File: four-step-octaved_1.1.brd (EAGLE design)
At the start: 94.3 x 44.4 mm, 39 parts, among them IC1 556, IC2 4017N, IC3 4040N, J1 -BATTERY+, J2 SPEAKER, U1 LM386N

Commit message: Rename RV to VR to match waltron
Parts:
- renumbered RV1 to VR1, RV2 to VR2, RV3 to VR3, RV4 to VR4, RV5 to VR5
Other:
- board text added: "VR1"
- board text added: "VR2"
- board text added: "VR3"
- board text added: "VR4"
- board text added: "VR5"
- board text added: "VR6"
- board text removed: "RV1"
- board text removed: "RV2"
- board text removed: "RV3"
- board text removed: "RV4"
- board text removed: "RV5"
- board text removed: "RV6"
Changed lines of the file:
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@@
 <text x="45.085" y="35.56" size="0.8128" layer="21" font="vector">C2</text>
 <text x="45.72" y="20.0025" size="0.8128" layer="21" font="vector">C3</text>
-<text x="82.55" y="37.7825" size="0.8128" layer="21" font="vector">RV1</text>
-<text x="82.8675" y="26.67" size="0.8128" layer="21" font="vector">RV6</text>
-<text x="17.145" y="7.9375" size="0.8128" layer="21" font="vector">RV2</text>
-<text x="32.7025" y="7.9375" size="0.8128" layer="21" font="vector">RV3</text>
-<text x="64.4525" y="7.9375" size="0.8128" layer="21" font="vector">RV5</text>
-<text x="48.5775" y="7.9375" size="0.8128" layer="21" font="vector">RV4</text>
+<text x="82.55" y="37.7825" size="0.8128" layer="21" font="vector">VR1</text>
+<text x="82.8675" y="26.67" size="0.8128" layer="21" font="vector">VR6</text>
+<text x="17.145" y="7.9375" size="0.8128" layer="21" font="vector">VR2</text>
+<text x="32.7025" y="7.9375" size="0.8128" layer="21" font="vector">VR3</text>
+<text x="64.4525" y="7.9375" size="0.8128" layer="21" font="vector">VR5</text>
+<text x="48.5775" y="7.9375" size="0.8128" layer="21" font="vector">VR4</text>
 <text x="62.865" y="31.115" size="0.8128" layer="21" font="vector">C5</text>
 <text x="84.7725" y="31.115" size="0.8128" layer="21" font="vector">TEMPO</text>
@@
 <attribute name="PROD_ID" value="RES-12182" x="67.6275" y="21.9075" size="1.778" layer="27" rot="R270" display="off"/>
 </element>
-<element name="RV1" library="SparkFun-Retired" package="TRIM_POT" value="50K" x="86.36" y="33.655" smashed="yes" rot="R90">
+<element name="VR1" library="SparkFun-Retired" package="TRIM_POT" value="50K" x="86.36" y="33.655" smashed="yes" rot="R90">
 <attribute name="PROD_ID" value="COM-00104" x="86.36" y="33.655" size="1.778" layer="27" rot="R90" display="off"/>
 </element>
-<element name="RV2" library="SparkFun-Retired" package="TRIM_POT" value="50K" x="15.24" y="3.175" smashed="yes" rot="R90">
+<element name="VR2" library="SparkFun-Retired" package="TRIM_POT" value="50K" x="15.24" y="3.175" smashed="yes" rot="R90">
 <attribute name="PROD_ID" value="COM-00104" x="15.24" y="3.175" size="1.778" layer="27" rot="R90" display="off"/>
 </element>
-<element name="RV3" library="SparkFun-Retired" package="TRIM_POT" value="50K" x="31.115" y="3.175" smashed="yes" rot="R90">
+<element name="VR3" library="SparkFun-Retired" package="TRIM_POT" value="50K" x="31.115" y="3.175" smashed="yes" rot="R90">
 <attribute name="PROD_ID" value="COM-00104" x="31.115" y="3.175" size="1.778" layer="27" rot="R90" display="off"/>
 </element>
-<element name="RV4" library="SparkFun-Retired" package="TRIM_POT" value="50K" x="46.99" y="3.175" smashed="yes" rot="R90">
+<element name="VR4" library="SparkFun-Retired" package="TRIM_POT" value="50K" x="46.99" y="3.175" smashed="yes" rot="R90">
 <attribute name="PROD_ID" value="COM-00104" x="46.99" y="3.175" size="1.778" layer="27" rot="R90" display="off"/>
 </element>
-<element name="RV5" library="SparkFun-Retired" package="TRIM_POT" value="50K" x="62.865" y="3.175" smashed="yes" rot="R90">
+<element name="VR5" library="SparkFun-Retired" package="TRIM_POT" value="50K" x="62.865" y="3.175" smashed="yes" rot="R90">
 <attribute name="PROD_ID" value="COM-00104" x="62.865" y="3.175" size="1.778" layer="27" rot="R90" display="off"/>
 </element>
@@
 <signal name="N$1" class="1">
 <contactref element="R1" pad="P$2"/>
-<contactref element="RV1" pad="3"/>
+<contactref element="VR1" pad="3"/>
 <wire x1="88.9" y1="33.655" x2="29.21" y2="27.6225" width="0" layer="19" extent="1-1"/>
 </signal>
 <signal name="N$2" class="1">
 <contactref element="IC1" pad="1"/>
-<contactref element="RV1" pad="2"/>
-<contactref element="RV1" pad="1"/>
+<contactref element="VR1" pad="2"/>
+<contactref element="VR1" pad="1"/>
 <contactref element="R2" pad="P$1"/>
 <wire x1="21.59" y1="30.7975" x2="32.0675" y2="35.56" width="0" layer="19" extent="1-1"/>
@@
 <signal name="N$9" class="1">
 <contactref element="IC2" pad="4"/>
-<contactref element="RV4" pad="3"/>
+<contactref element="VR4" pad="3"/>
 <contactref element="R7" pad="P$2"/>
 <wire x1="49.53" y1="3.175" x2="48.26" y2="10.795" width="0" layer="19" extent="1-1"/>
@@
 <signal name="N$10" class="1">
 <contactref element="IC2" pad="7"/>
-<contactref element="RV5" pad="3"/>
+<contactref element="VR5" pad="3"/>
 <contactref element="R8" pad="P$2"/>
 <wire x1="65.405" y1="3.175" x2="64.135" y2="10.795" width="0" layer="19" extent="1-1"/>
@@
 <signal name="N$7" class="1">
 <contactref element="IC2" pad="3"/>
-<contactref element="RV2" pad="3"/>
+<contactref element="VR2" pad="3"/>
 <contactref element="R5" pad="P$2"/>
 <wire x1="16.51" y1="10.795" x2="4.7625" y2="31.75" width="0" layer="19" extent="1-1"/>
@@
 <signal name="N$8" class="1">
 <contactref element="IC2" pad="2"/>
-<contactref element="RV3" pad="3"/>
+<contactref element="VR3" pad="3"/>
 <contactref element="R6" pad="P$2"/>
 <wire x1="33.655" y1="3.175" x2="32.385" y2="10.795" width="0" layer="19" extent="1-1"/>
@@
 </signal>
 <signal name="N$11" class="1">
-<contactref element="RV2" pad="1"/>
-<contactref element="RV2" pad="2"/>
+<contactref element="VR2" pad="1"/>
+<contactref element="VR2" pad="2"/>
 <contactref element="D1" pad="A"/>
 <wire x1="12.7" y1="3.175" x2="15.24" y2="8.255" width="0" layer="19" extent="1-1"/>
@@
 </signal>
 <signal name="N$16" class="1">
-<contactref element="RV3" pad="1"/>
-<contactref element="RV3" pad="2"/>
+<contactref element="VR3" pad="1"/>
+<contactref element="VR3" pad="2"/>
 <contactref element="D3" pad="A"/>
 <wire x1="28.575" y1="3.175" x2="31.115" y2="8.255" width="0" layer="19" extent="1-1"/>
@@
 </signal>
 <signal name="N$18" class="1">
-<contactref element="RV5" pad="1"/>
-<contactref element="RV5" pad="2"/>
+<contactref element="VR5" pad="1"/>
+<contactref element="VR5" pad="2"/>
 <contactref element="D7" pad="A"/>
 <wire x1="60.325" y1="3.175" x2="62.865" y2="8.255" width="0" layer="19" extent="1-1"/>
@@
 </signal>
 <signal name="N$17" class="1">
-<contactref element="RV4" pad="1"/>
-<contactref element="RV4" pad="2"/>
+<contactref element="VR4" pad="1"/>
+<contactref element="VR4" pad="2"/>
 <contactref element="D5" pad="A"/>
 <wire x1="44.45" y1="3.175" x2="46.99" y2="8.255" width="0" layer="19" extent="1-1"/>

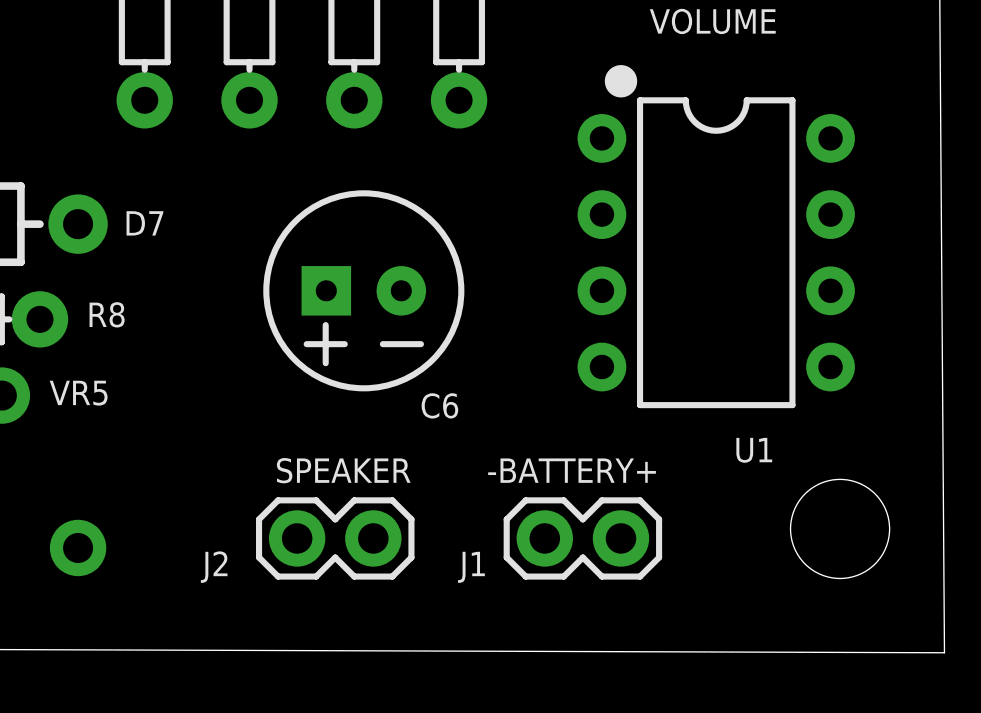
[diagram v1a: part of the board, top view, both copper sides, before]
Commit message: Add switch
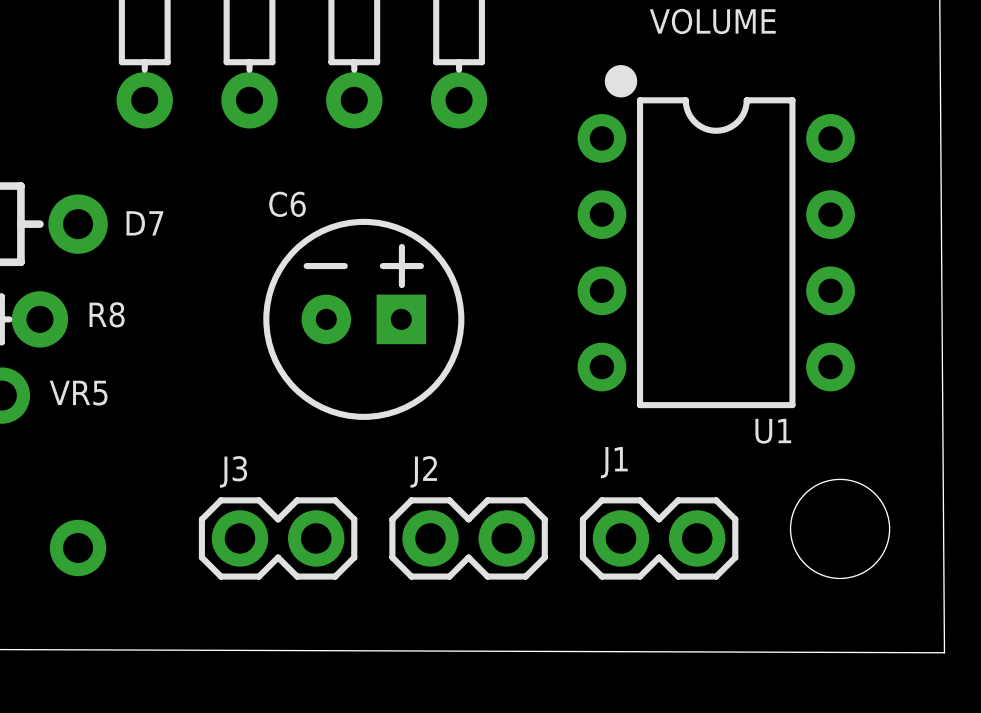
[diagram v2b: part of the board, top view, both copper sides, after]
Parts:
- added J3: SPEAKER, SparkFun-Connectors:1X02
- J1: value -BATTERY+ -> (none)
- J2: value SPEAKER -> -BATTERY+
- moved J2 4.44 mm to (79.7, 3.49)
- moved J1 2.54 mm to (86.0, 3.49)
- moved C6 0.95 mm to (74.9, 10.8), turned to 0 degrees
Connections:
- new net N$32: J1.2, J2.1
- net GND: now also J3.2; no longer J1.2
- net N$27: now also J3.1; no longer J2.1

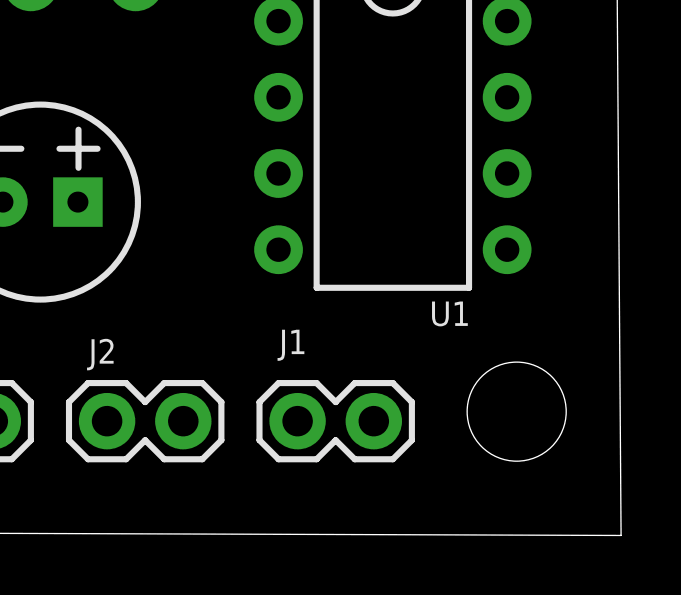
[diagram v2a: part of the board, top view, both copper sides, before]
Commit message: Update 386 name
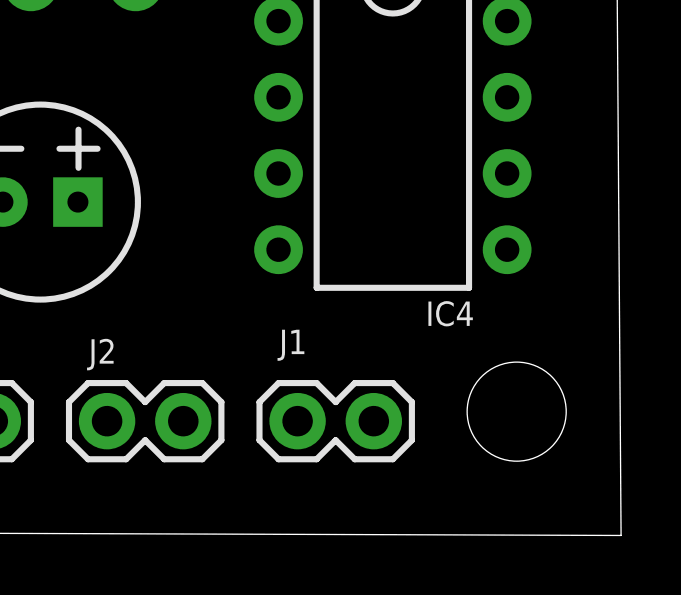
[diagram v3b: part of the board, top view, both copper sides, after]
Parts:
- renumbered U1 to IC4
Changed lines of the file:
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@@
 <attribute name="PROD_ID" value="COM-00104" x="86.6775" y="22.86" size="1.778" layer="27" rot="R90" display="off"/>
 </element>
-<element name="U1" library="SparkFun-IC-Amplifiers" package="DIP08" value="LM386N" x="86.6775" y="13.0175" smashed="yes" rot="R270">
+<element name="IC4" library="SparkFun-IC-Amplifiers" package="DIP08" value="LM386N" x="86.6775" y="13.0175" smashed="yes" rot="R270">
 <attribute name="NAME" x="88.5825" y="6.6675" size="0.8128" layer="25" font="vector" align="bottom-center"/>
 <attribute name="PROD_ID" value="IC-10899" x="86.6775" y="13.0175" size="1.778" layer="27" rot="R270" display="off"/>
@@
 <contactref element="IC2" pad="16"/>
 <contactref element="C4" pad="1"/>
-<contactref element="U1" pad="6"/>
+<contactref element="IC4" pad="6"/>
 <contactref element="IC3" pad="16"/>
 <contactref element="C5" pad="1"/>
@@
 <signal name="N$24" class="1">
 <contactref element="RV6" pad="1"/>
-<contactref element="U1" pad="3"/>
+<contactref element="IC4" pad="3"/>
 <wire x1="82.8675" y1="11.7475" x2="86.6775" y2="27.94" width="0" layer="19" extent="1-1"/>
 </signal>
@@
 <signal name="N$28" class="1">
 <contactref element="C6" pad="1"/>
-<contactref element="U1" pad="5"/>
+<contactref element="IC4" pad="5"/>
 <wire x1="76.18" y1="10.795" x2="90.4875" y2="9.2075" width="0" layer="19" extent="1-1"/>
 </signal>
@@
 <contactref element="IC3" pad="11"/>
 <contactref element="RV6" pad="2"/>
-<contactref element="U1" pad="2"/>
-<contactref element="U1" pad="4"/>
+<contactref element="IC4" pad="2"/>
+<contactref element="IC4" pad="4"/>
 <contactref element="J3" pad="2"/>
 <contactref element="D2" pad="K"/>

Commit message: Autoroute, finish
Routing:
- net GND: track 0.00 -> 229.7 mm
- net +9V: track 0.00 -> 121.6 mm
- net N$10: track 0.00 -> 78.2 mm
- net N$2: track 0.00 -> 74.6 mm
- net N$19: track 0.00 -> 69.6 mm
- net N$1: track 0.00 -> 67.3 mm
- net N$9: track 0.00 -> 62.1 mm
- net N$8: track 0.00 -> 55.9 mm
- net N$7: track 0.00 -> 34.0 mm
- net N$25: track 0.00 -> 31.7 mm
- net N$5: track 0.00 -> 31.4 mm
- net N$31: track 0.00 -> 26.7 mm
- net N$21: track 0.00 -> 26.1 mm
- net N$22: track 0.00 -> 21.6 mm
- net N$43: track 0.00 -> 21.5 mm
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
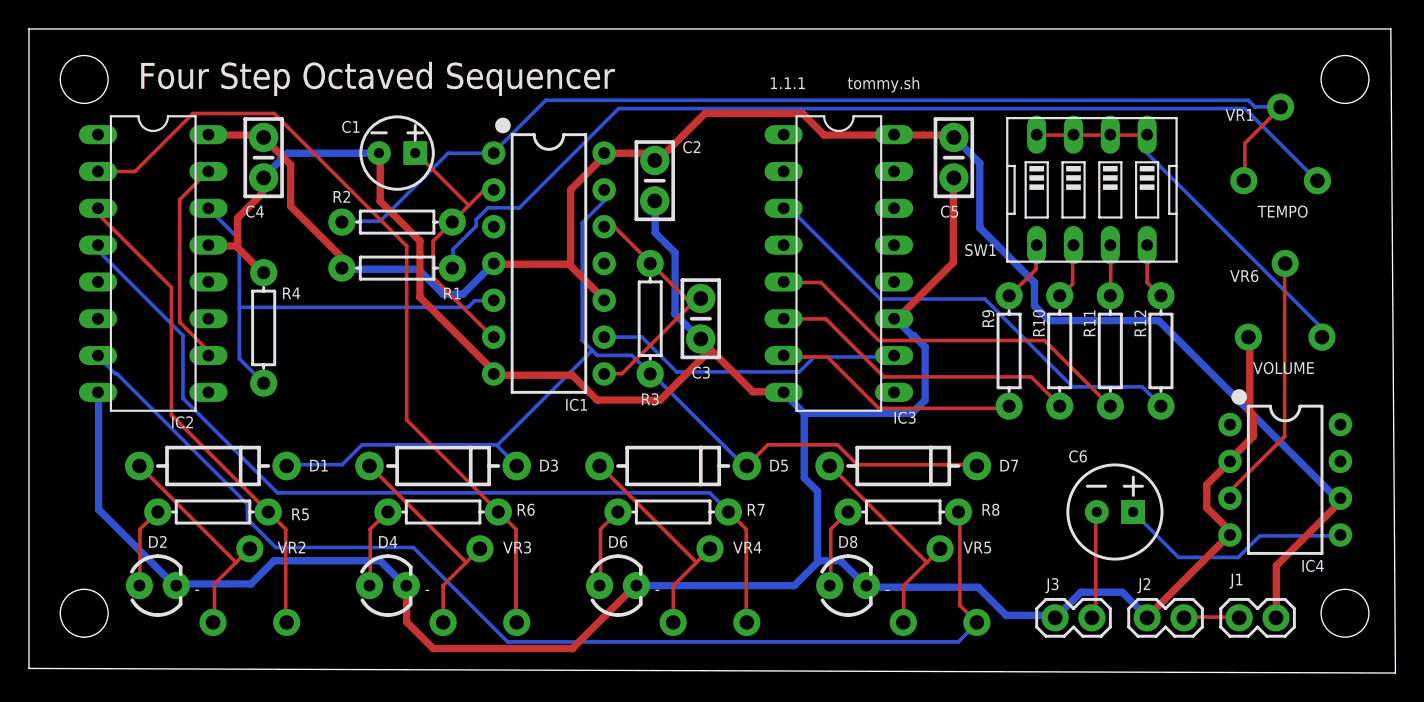
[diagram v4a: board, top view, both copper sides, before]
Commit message: Update to 1.1.2
- Add header label text
- Indicate battery and speaker polarity
- Reverse order octave switches: low to high = left to right
- Label ICs
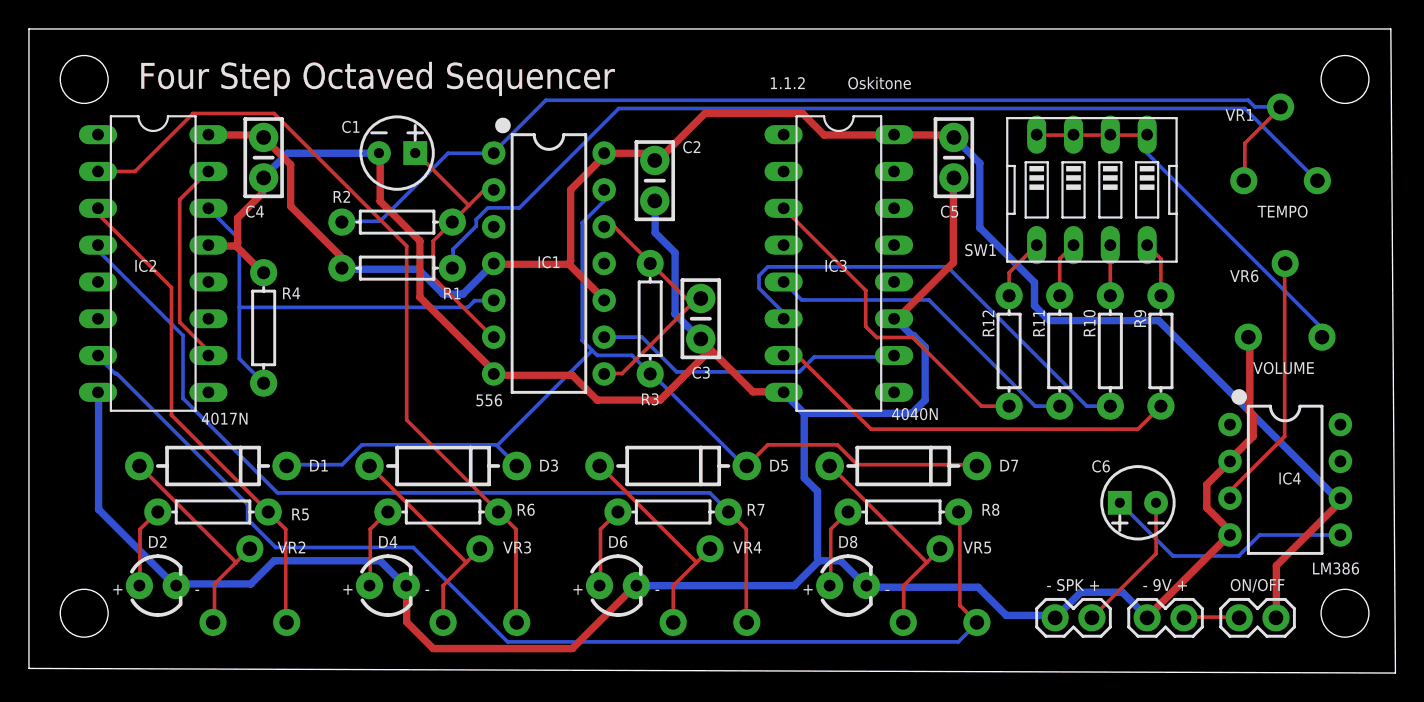
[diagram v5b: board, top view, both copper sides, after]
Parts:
- C6: device SparkFun-Capacitors:CPOL-RADIAL-2.5MM-6.5MM -> SparkFun-Capacitors:CPOL-RADIAL-2.5MM-5MM
- IC4: value LM386N -> LM386
- J1: value (none) -> ON/OFF
- J2: value -BATTERY+ -> - 9V +
- J3: value SPEAKER -> - SPK +
- moved R12 10.5 mm to (67.6, 21.9)
- moved R9 10.5 mm to (78.1, 21.9)
- moved R10 3.49 mm to (74.6, 21.9)
- moved R11 3.49 mm to (71.1, 21.9)
- moved C6 1.71 mm to (76.5, 11.4), turned to 180 degrees
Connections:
- net N$23: now also R12.P$1, SW1.5; no longer R10.P$1, SW1.6
- net N$26: now also SW1.6; no longer SW1.7
- net N$29: now also R10.P$1, SW1.7; no longer R9.P$1, SW1.5
- net N$30: now also R9.P$1; no longer R12.P$1
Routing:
- net N$20: track 17.1 -> 28.8 mm
- net N$22: track 21.6 -> 32.2 mm
- net N$25: track 31.7 -> 22.7 mm
- net N$21: track 26.1 -> 22.6 mm
- net N$27: track 7.45 -> 9.77 mm
- net N$28: track 16.2 -> 17.3 mm
- net N$29: track 4.30 -> 3.49 mm
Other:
- board text added: "+"
- board text added: "1.1.2"
- board text added: "Oskitone"
- board text removed: "1.1.1"
- board text removed: "tommy.sh"
